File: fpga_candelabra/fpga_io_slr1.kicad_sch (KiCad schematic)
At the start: 1 part, among them U1 XCVU13P-B2104

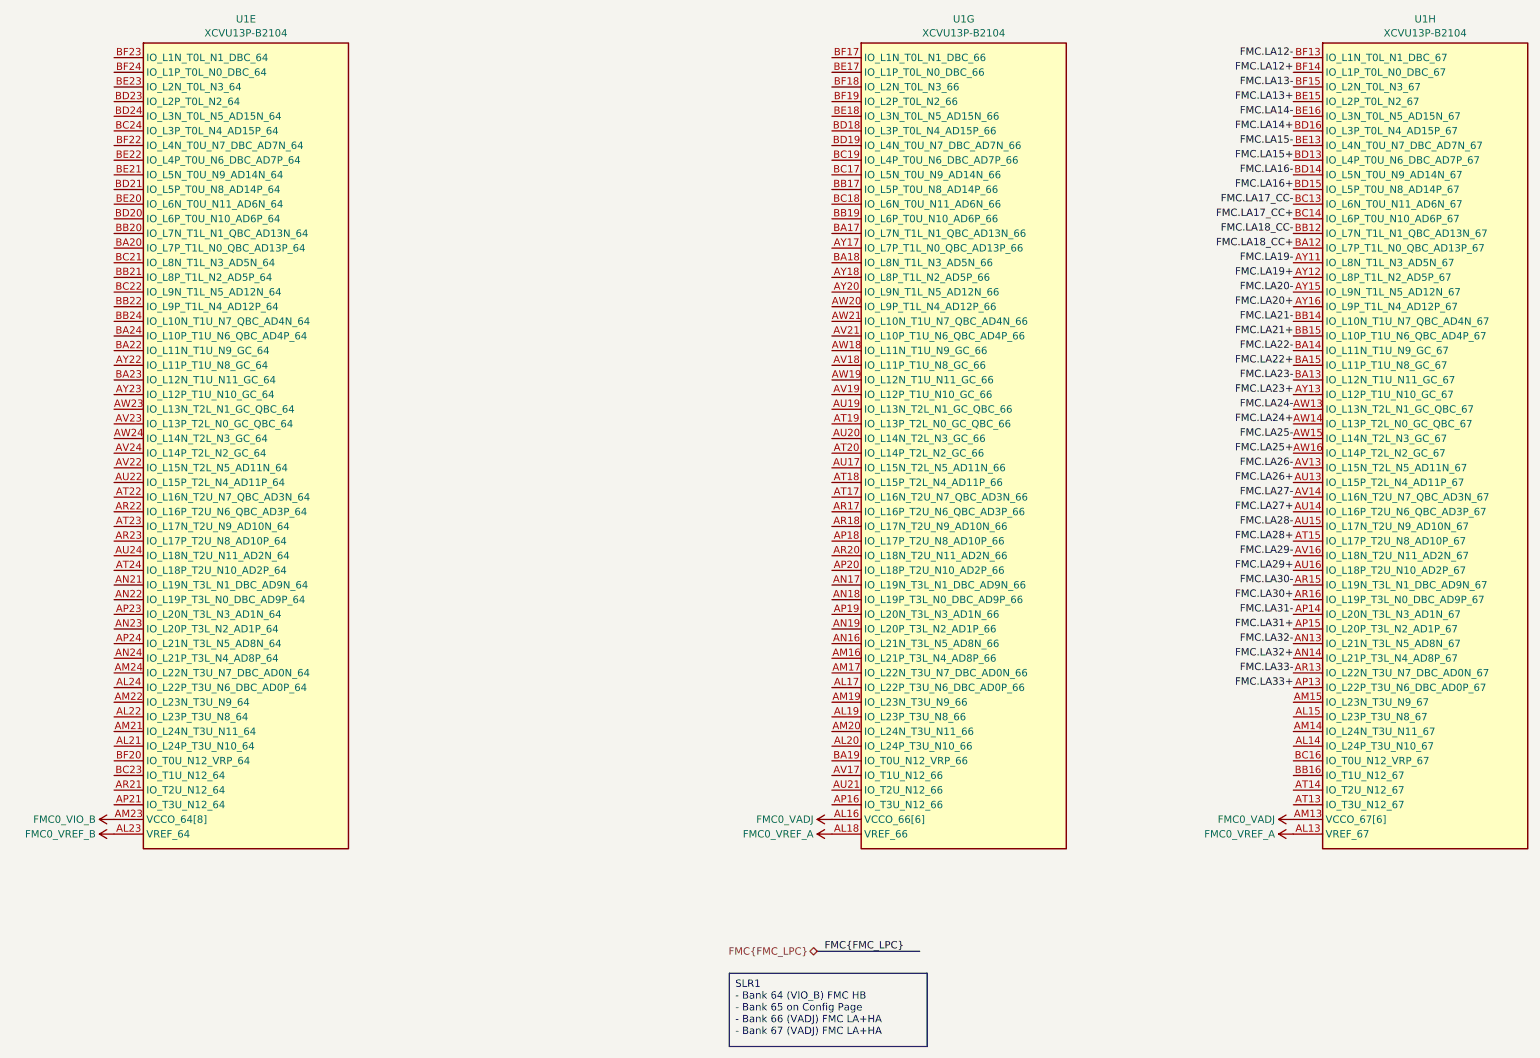
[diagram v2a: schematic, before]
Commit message: fpga_candelabra: sch & layout v0.5, pass basic ERC & DRC
Signed-off-by: Yichuan Gao <gaoyichuan000@gmail.com>
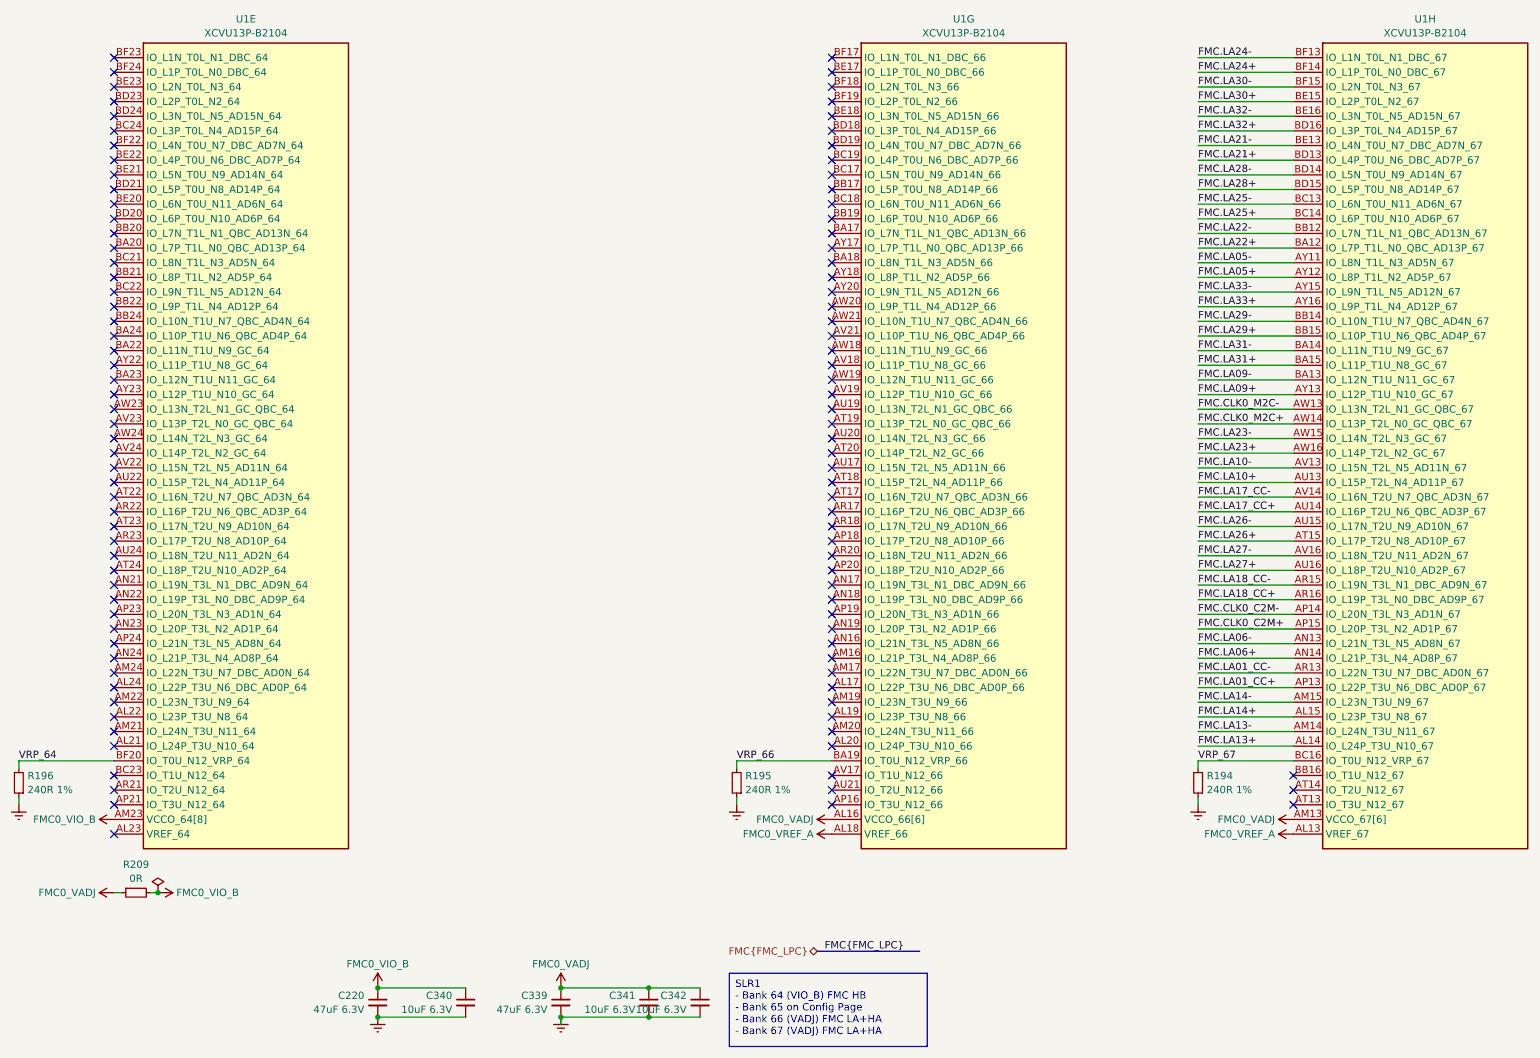
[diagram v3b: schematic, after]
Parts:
- added C220, C339: 47uF 6.3V, Capacitor_SMD:C_0603_1608Metric, symbol Device:C_Small
- added C340, C341, C342: 10uF 6.3V, Capacitor_SMD:C_0402_1005Metric, symbol Device:C_Small
- added R194, R195, R196: 240R 1%, Resistor_SMD:R_0402_1005Metric, symbol Device:R_Small
- added R209: 0R, Resistor_SMD:R_0402_1005Metric, symbol Device:R_Small
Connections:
- net FMC.LA12+ is gone; now on net FMC.LA24+: U1.BF14 (IO_L1P_T0L_N0_DBC_67)
- net FMC.LA12- is gone; now on net FMC.LA24-: U1.BF13 (IO_L1N_T0L_N1_DBC_67)
- net FMC.LA15+ is gone; now on net FMC.LA21+: U1.BD13 (IO_L4P_T0U_N6_DBC_AD7P_67)
- net FMC.LA15- is gone; now on net FMC.LA21-: U1.BE13 (IO_L4N_T0U_N7_DBC_AD7N_67)
- net FMC.LA16+ is gone; now on net FMC.LA28+: U1.BD15 (IO_L5P_T0U_N8_AD14P_67)
- net FMC.LA16- is gone; now on net FMC.LA28-: U1.BD14 (IO_L5N_T0U_N9_AD14N_67)
- net FMC.LA20+ is gone; now on net FMC.LA33+: U1.AY16 (IO_L9P_T1L_N4_AD12P_67)
- net FMC.LA20- is gone; now on net FMC.LA33-: U1.AY15 (IO_L9N_T1L_N5_AD12N_67)
- net FMC.LA13+: now also U1.AL14 (IO_L24P_T3U_N10_67); no longer U1.BE15 (IO_L2P_T0L_N2_67)
- net FMC.LA13-: now also U1.AM14 (IO_L24N_T3U_N11_67); no longer U1.BF15 (IO_L2N_T0L_N3_67)
- net FMC.LA14+: now also U1.AL15 (IO_L23P_T3U_N8_67); no longer U1.BD16 (IO_L3P_T0L_N4_AD15P_67)
- net FMC.LA14-: now also U1.AM15 (IO_L23N_T3U_N9_67); no longer U1.BE16 (IO_L3N_T0L_N5_AD15N_67)
- net FMC.LA17_CC+: now also U1.AU14 (IO_L16P_T2U_N6_QBC_AD3P_67); no longer U1.BC14 (IO_L6P_T0U_N10_AD6P_67)
- net FMC.LA17_CC-: now also U1.AV14 (IO_L16N_T2U_N7_QBC_AD3N_67); no longer U1.BC13 (IO_L6N_T0U_N11_AD6N_67)
- net FMC.LA18_CC+: now also U1.AR16 (IO_L19P_T3L_N0_DBC_AD9P_67); no longer U1.BA12 (IO_L7P_T1L_N0_QBC_AD13P_67)
- net FMC.LA18_CC-: now also U1.AR15 (IO_L19N_T3L_N1_DBC_AD9N_67); no longer U1.BB12 (IO_L7N_T1L_N1_QBC_AD13N_67)
- net FMC.LA21+: no longer U1.BB15 (IO_L10P_T1U_N6_QBC_AD4P_67)
- net FMC.LA21-: no longer U1.BB14 (IO_L10N_T1U_N7_QBC_AD4N_67)
- net FMC.LA22+: now also U1.BA12 (IO_L7P_T1L_N0_QBC_AD13P_67); no longer U1.BA15 (IO_L11P_T1U_N8_GC_67)
- net FMC.LA22-: now also U1.BB12 (IO_L7N_T1L_N1_QBC_AD13N_67); no longer U1.BA14 (IO_L11N_T1U_N9_GC_67)
- net FMC.LA23+: now also U1.AW16 (IO_L14P_T2L_N2_GC_67); no longer U1.AY13 (IO_L12P_T1U_N10_GC_67)
- net FMC.LA23-: now also U1.AW15 (IO_L14N_T2L_N3_GC_67); no longer U1.BA13 (IO_L12N_T1U_N11_GC_67)
- net FMC.LA24+: no longer U1.AW14 (IO_L13P_T2L_N0_GC_QBC_67)
- net FMC.LA24-: no longer U1.AW13 (IO_L13N_T2L_N1_GC_QBC_67)
- net FMC.LA25+: now also U1.BC14 (IO_L6P_T0U_N10_AD6P_67); no longer U1.AW16 (IO_L14P_T2L_N2_GC_67)
- net FMC.LA25-: now also U1.BC13 (IO_L6N_T0U_N11_AD6N_67); no longer U1.AW15 (IO_L14N_T2L_N3_GC_67)
- net FMC.LA26+: now also U1.AT15 (IO_L17P_T2U_N8_AD10P_67); no longer U1.AU13 (IO_L15P_T2L_N4_AD11P_67)
- net FMC.LA26-: now also U1.AU15 (IO_L17N_T2U_N9_AD10N_67); no longer U1.AV13 (IO_L15N_T2L_N5_AD11N_67)
- net FMC.LA27+: now also U1.AU16 (IO_L18P_T2U_N10_AD2P_67); no longer U1.AU14 (IO_L16P_T2U_N6_QBC_AD3P_67)
- net FMC.LA27-: now also U1.AV16 (IO_L18N_T2U_N11_AD2N_67); no longer U1.AV14 (IO_L16N_T2U_N7_QBC_AD3N_67)
- net FMC.LA28+: no longer U1.AT15 (IO_L17P_T2U_N8_AD10P_67)
- net FMC.LA28-: no longer U1.AU15 (IO_L17N_T2U_N9_AD10N_67)
- net FMC.LA29+: now also U1.BB15 (IO_L10P_T1U_N6_QBC_AD4P_67); no longer U1.AU16 (IO_L18P_T2U_N10_AD2P_67)
- net FMC.LA29-: now also U1.BB14 (IO_L10N_T1U_N7_QBC_AD4N_67); no longer U1.AV16 (IO_L18N_T2U_N11_AD2N_67)
- net FMC.LA30+: now also U1.BE15 (IO_L2P_T0L_N2_67); no longer U1.AR16 (IO_L19P_T3L_N0_DBC_AD9P_67)
- net FMC.LA30-: now also U1.BF15 (IO_L2N_T0L_N3_67); no longer U1.AR15 (IO_L19N_T3L_N1_DBC_AD9N_67)
- net FMC.LA31+: now also U1.BA15 (IO_L11P_T1U_N8_GC_67); no longer U1.AP15 (IO_L20P_T3L_N2_AD1P_67)
- net FMC.LA31-: now also U1.BA14 (IO_L11N_T1U_N9_GC_67); no longer U1.AP14 (IO_L20N_T3L_N3_AD1N_67)
- net FMC.LA32+: now also U1.BD16 (IO_L3P_T0L_N4_AD15P_67); no longer U1.AN14 (IO_L21P_T3L_N4_AD8P_67)
- net FMC.LA32-: now also U1.BE16 (IO_L3N_T0L_N5_AD15N_67); no longer U1.AN13 (IO_L21N_T3L_N5_AD8N_67)
- net FMC.LA33+: no longer U1.AP13 (IO_L22P_T3U_N6_DBC_AD0P_67)
- net FMC.LA33-: no longer U1.AR13 (IO_L22N_T3U_N7_DBC_AD0N_67)
- net FMC0_VADJ: now also C339.1, C341.1, C342.1, R209.1
- net FMC0_VIO_B: now also C220.1, C340.1, R209.2
- net VRP_67: now reaches U1.BC16 (IO_T0U_N12_VRP_67)
- net VRP_67: now also R194.2
- net VRP_64: now reaches U1.BF20 (IO_T0U_N12_VRP_64)
- net VRP_64: now also R196.2
- net VRP_66: now reaches U1.BA19 (IO_T0U_N12_VRP_66)
- net VRP_66: now also R195.2
- net FMC.LA19+ renamed FMC.LA05+
- net FMC.LA19- renamed FMC.LA05-
- net FMC0_VREF_B: no longer names the net of U1.AL23 (VREF_64)
- new net Earth: C220.2, C339.2, C340.2, C341.2, C342.2, R194.1, R195.1, R196.1
- new net FMC.CLK0_C2M+: U1.AP15 (IO_L20P_T3L_N2_AD1P_67)
- new net FMC.CLK0_C2M-: U1.AP14 (IO_L20N_T3L_N3_AD1N_67)
- new net FMC.CLK0_M2C+: U1.AW14 (IO_L13P_T2L_N0_GC_QBC_67)
- new net FMC.CLK0_M2C-: U1.AW13 (IO_L13N_T2L_N1_GC_QBC_67)
- new net FMC.LA01_CC+: U1.AP13 (IO_L22P_T3U_N6_DBC_AD0P_67)
- new net FMC.LA01_CC-: U1.AR13 (IO_L22N_T3U_N7_DBC_AD0N_67)
- new net FMC.LA06+: U1.AN14 (IO_L21P_T3L_N4_AD8P_67)
- new net FMC.LA06-: U1.AN13 (IO_L21N_T3L_N5_AD8N_67)
- new net FMC.LA09+: U1.AY13 (IO_L12P_T1U_N10_GC_67)
- new net FMC.LA09-: U1.BA13 (IO_L12N_T1U_N11_GC_67)
- new net FMC.LA10+: U1.AU13 (IO_L15P_T2L_N4_AD11P_67)
- new net FMC.LA10-: U1.AV13 (IO_L15N_T2L_N5_AD11N_67)
- no-connect marks 0 -> 106

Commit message: fpga_candelabra: add author & rev to schematics
Signed-off-by: Yichuan Gao <gaoyichuan000@gmail.com>
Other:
- company: (none) -> CHIPS Alliance
- title: (none) -> FPGA SLR1 IO
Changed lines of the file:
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@@
 	(generator_version "8.0")
 	(paper "A4")
+	(title_block
+		(title "FPGA SLR1 IO")
+		(date "2025-02-05")
+		(rev "0.2.0")
+		(company "CHIPS Alliance")
+		(comment 1 "Yichuan Gao")
+		(comment 2 "Yichuan Gao")
+	)
 	(junction
 		(at 127 186.69)

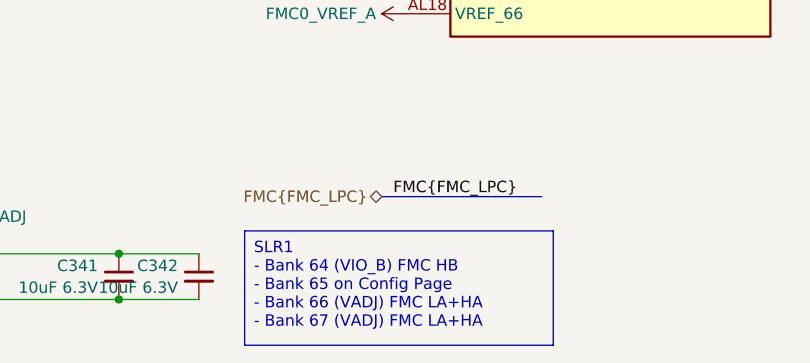
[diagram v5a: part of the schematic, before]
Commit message: fpga_candelabra: update to kicad 9.0
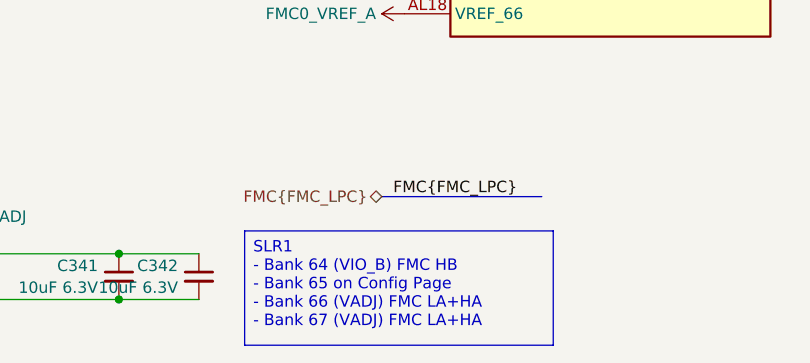
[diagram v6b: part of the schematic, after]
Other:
- company: CHIPS Alliance -> Sipeed
